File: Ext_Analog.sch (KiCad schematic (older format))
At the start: 27 parts

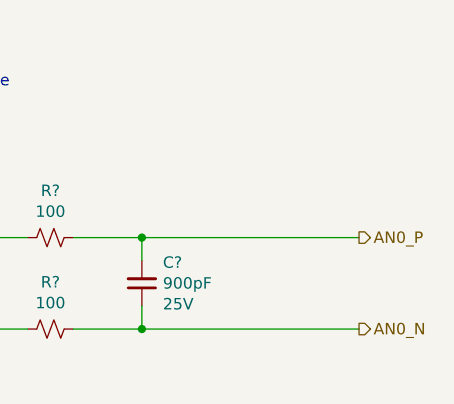
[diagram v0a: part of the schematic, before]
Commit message: Completed LED_Comm Completed Ext_Analog Added AWG and ADC sheets
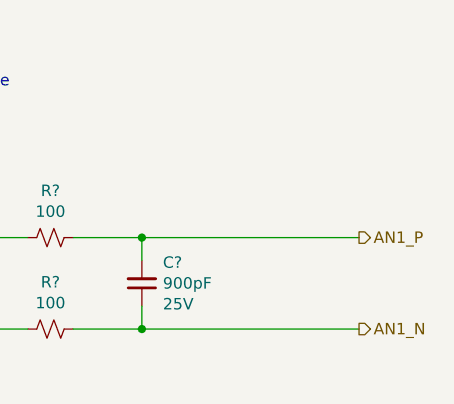
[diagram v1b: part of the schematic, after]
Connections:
- net labels added: AN1_N, AN1_P
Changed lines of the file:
@@
 $Descr A4 11693 8268
 encoding utf-8
-Sheet 15 18
+Sheet 17 19
 Title ""
 Date ""
@@
 Depends on the input voltage
 Text HLabel 9250 4750 2    50   Output ~ 0
-AN0_P
+AN1_P
 Text HLabel 9250 5150 2    50   Output ~ 0
-AN0_N
+AN1_N
 $EndSCHEMATC
